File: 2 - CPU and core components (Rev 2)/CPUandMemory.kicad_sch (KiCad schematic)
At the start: 10 parts

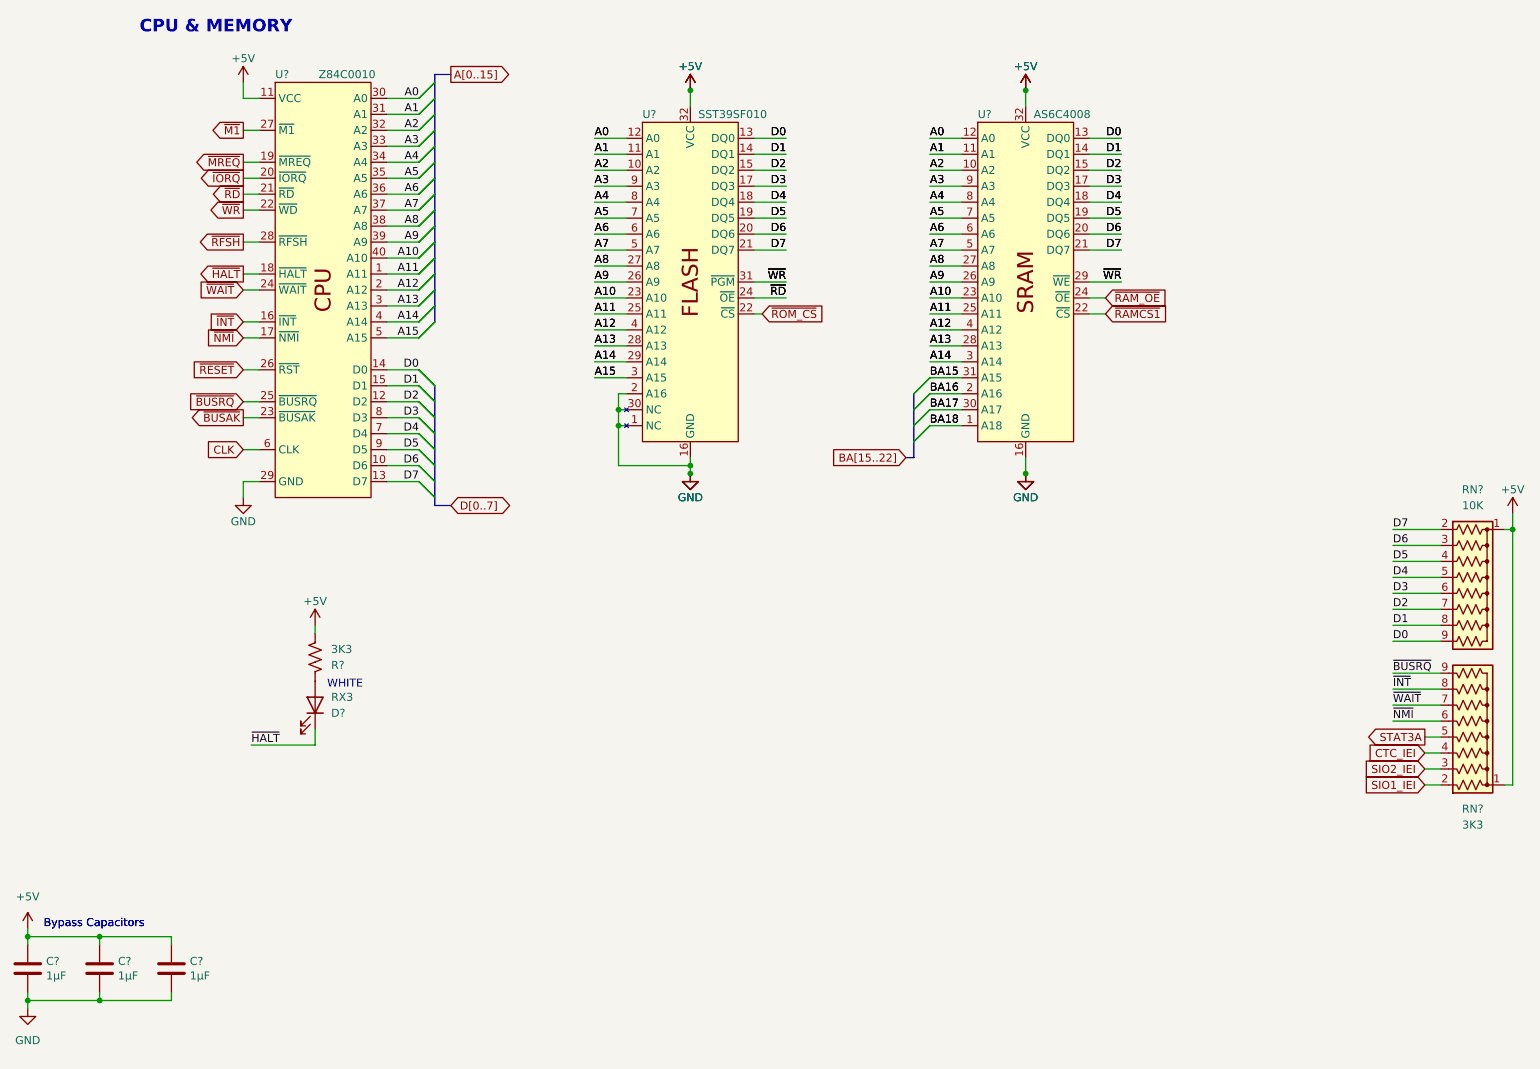
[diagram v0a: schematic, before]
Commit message: Replacing a lot of TTL chips by 2 PLDs. Also, added blinkenlights.
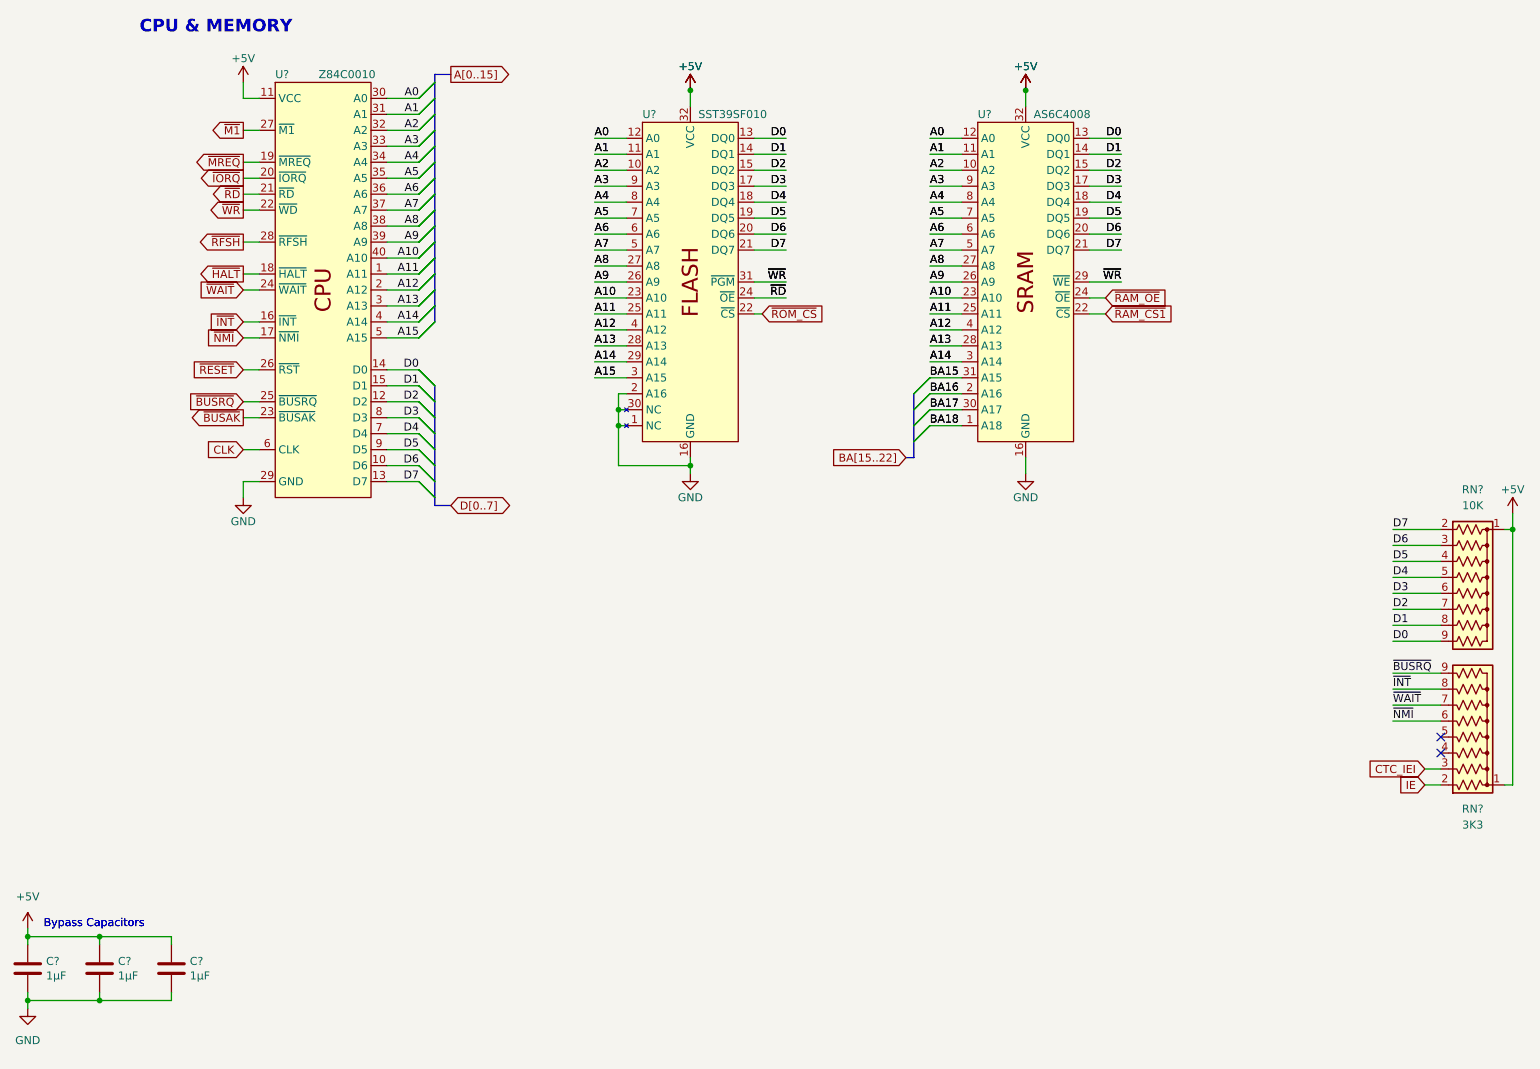
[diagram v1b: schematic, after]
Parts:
- removed D?: RX3, LED_THT:LED_D3.0mm_Horizontal_O1.27mm_Z2.0mm_Clear, symbol Device:LED
- removed R?: 3K3, Resistor_THT:R_Axial_DIN0207_L6.3mm_D2.5mm_P10.16mm_Horizontal, symbol Device:R_US
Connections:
- net SIO2_IEI is gone; now on net CTC_IEI: RN?.3 (R2)
- net CTC_IEI: no longer RN?.4 (R3)
- net SIO1_IEI renamed IE
- net STAT3A: no longer names the net of RN?.5 (R4)
- net ~{RAMCS1} renamed ~{RAM_CS1}
- no-connect marks 0 -> 2
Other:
- note removed: "WHITE"

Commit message: Added Interrupt Enable daisy chain jumpers between the ISA slots
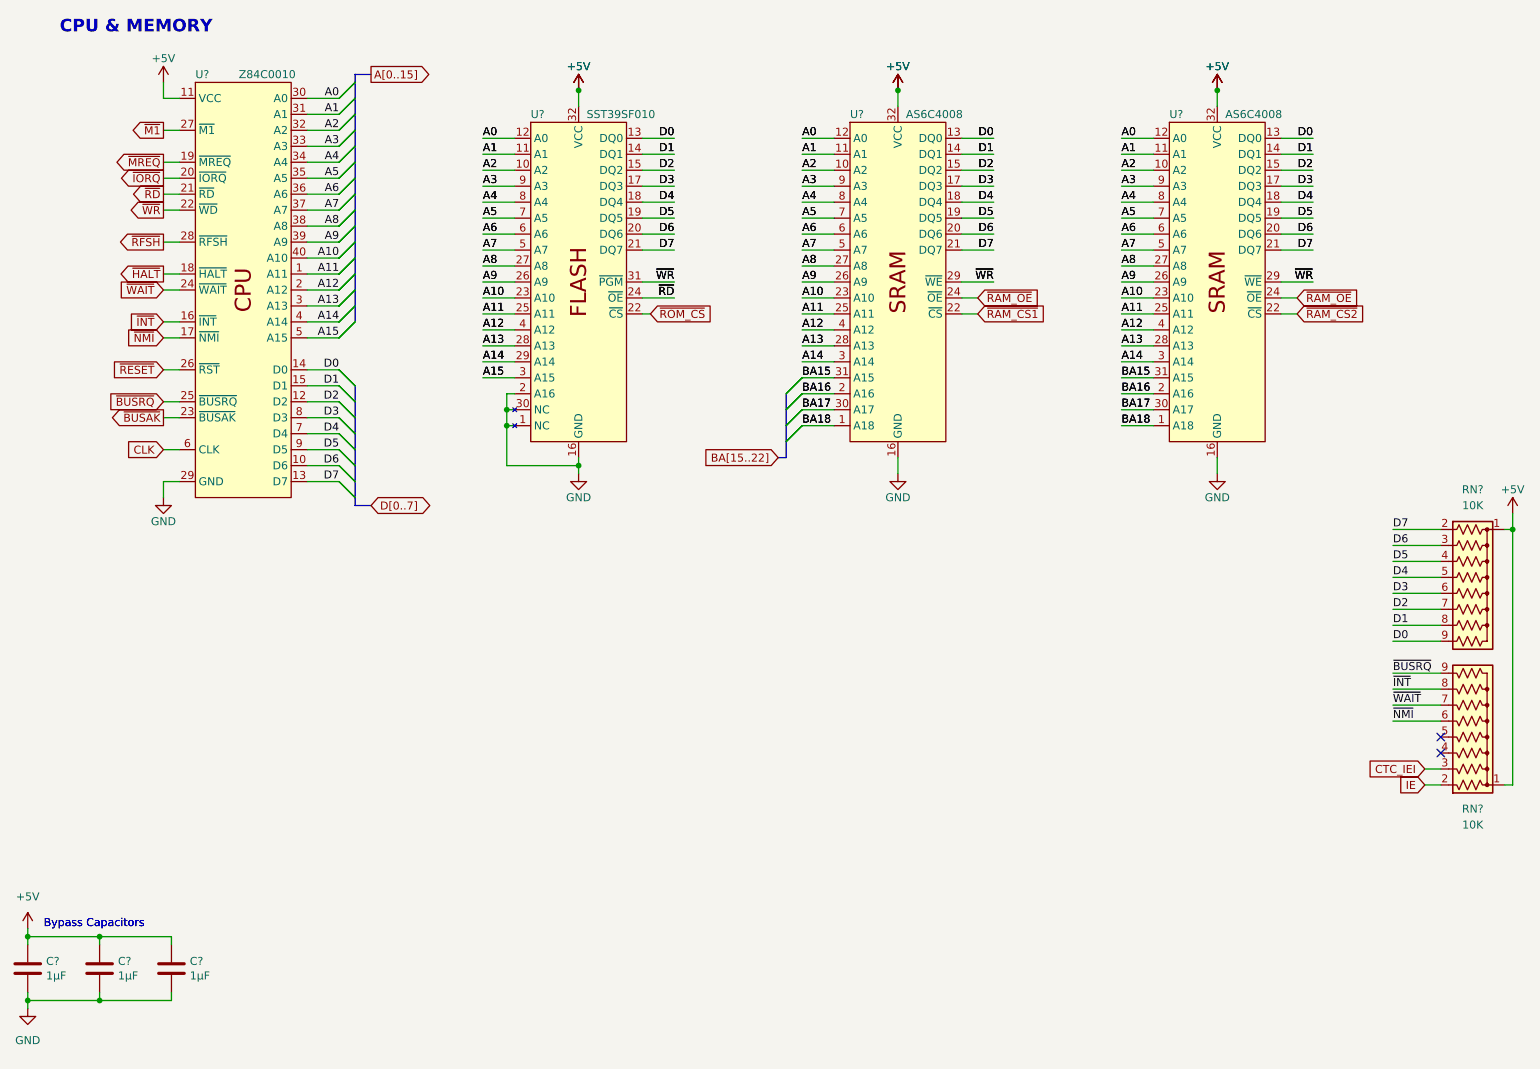
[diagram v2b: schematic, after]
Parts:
- added U?: AS6C4008, Package_DIP:DIP-32_W15.24mm_Socket, symbol 0_Library:AS6C4008
- RN?: value 3K3 -> 10K
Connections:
- net +5V: now also U?.32 (VCC)
- net A0: now also U?.12 (A0)
- net A1: now also U?.11 (A1)
- net A10: now also U?.23 (A10)
- net A11: now also U?.25 (A11)
- net A12: now also U?.4 (A12)
- net A13: now also U?.28 (A13)
- net A14: now also U?.3 (A14)
- net A2: now also U?.10 (A2)
- net A3: now also U?.9 (A3)
- net A4: now also U?.8 (A4)
- net A5: now also U?.7 (A5)
- net A6: now also U?.6 (A6)
- net A7: now also U?.5 (A7)
- net A8: now also U?.27 (A8)
- net A9: now also U?.26 (A9)
- net BA15: now also U?.31 (A15)
- net BA16: now also U?.2 (A16)
- net BA17: now also U?.30 (A17)
- net BA18: now also U?.1 (A18)
- net D0: now also U?.13 (DQ0)
- net D1: now also U?.14 (DQ1)
- net D2: now also U?.15 (DQ2)
- net D3: now also U?.17 (DQ3)
- net D4: now also U?.18 (DQ4)
- net D5: now also U?.19 (DQ5)
- net D6: now also U?.20 (DQ6)
- net D7: now also U?.21 (DQ7)
- net GND: now also U?.16 (GND)
- net ~{RAM_OE}: now also U?.24 (~{OE})
- net ~{WR}: now also U?.29 (~{WE})
- new net ~{RAM_CS2}: U?.22 (~{CS})
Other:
- title: Main board with basic peripherals -> CPU with Flash ROM and RAM
- moved on the sheet: U?

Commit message: Finished component placement, currently routing.
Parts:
- removed U?: AS6C4008, Package_DIP:DIP-32_W15.24mm_Socket, symbol 0_Library:AS6C4008
- RN?: value 10K -> 3K3
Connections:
- net CTC_IEI: now also RN?.7 (R6); no longer RN?.3 (R2)
- net IE: now also RN?.6 (R5); no longer RN?.2 (R1)
- net ~{BUSRQ}: now also RN?.5 (R4); no longer RN?.9 (R8)
- net ~{INT}: now also RN?.3 (R2); no longer RN?.8 (R7)
- net ~{NMI}: now also RN?.2 (R1); no longer RN?.6 (R5)
- net ~{WAIT}: now also RN?.4 (R3); no longer RN?.7 (R6)
- net ~{RAM_CS1} renamed ~{RAM_CS}
- new net R_FTRA: RN?.9 (R8)
- new net R_FTRB: RN?.8 (R7)
- no-connect marks 2 -> 0
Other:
- moved on the sheet: RN?, U?
